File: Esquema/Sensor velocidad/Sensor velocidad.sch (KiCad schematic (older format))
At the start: 1 part

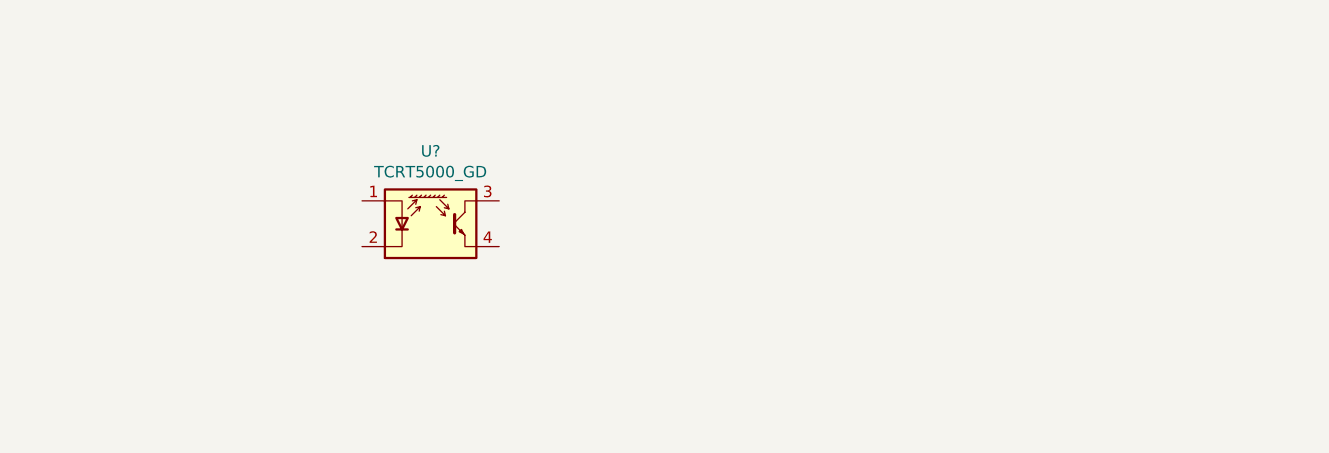
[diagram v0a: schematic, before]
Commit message: Coloco componentes en esquema.
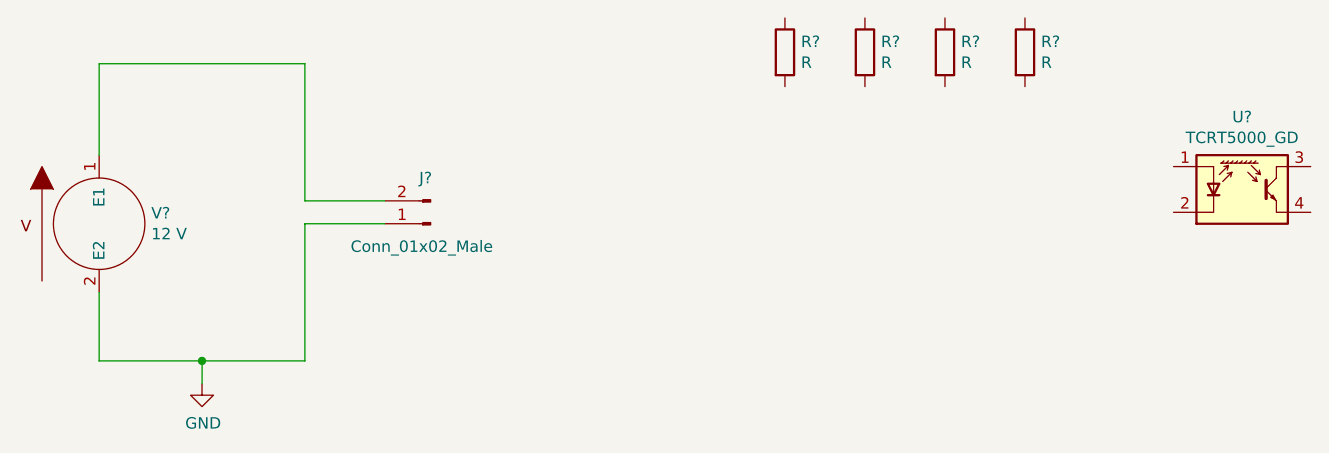
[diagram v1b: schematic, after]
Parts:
- added J?: Conn_01x02_Male, symbol Connector:Conn_01x02_Male
- added R? (x4): R, symbol Device:R
- added V?: 12 V, symbol pspice:VSOURCE
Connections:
- new net: J?.2 (Pin_2), V?.1 (E1)
- new net GND: J?.1 (Pin_1), V?.2 (E2)
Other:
- moved on the sheet: U?
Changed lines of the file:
@@
 EESchema Schematic File Version 4
-EELAYER 30 0
+LIBS:Sensor velocidad-cache
+EELAYER 29 0
 EELAYER END
 $Descr A4 11693 8268
@@
 L Sensor_vel_bib:TCRT5000_GD U?
 U 1 1 5D8A6EC4
-P 4450 2250
-F 0 "U?" H 4450 2567 50  0000 C CNN
-F 1 "TCRT5000_GD" H 4450 2476 50  0000 C CNN
-F 2 "" H 4450 2050 50  0001 C CNN
-F 3 "https://www.vishay.com/docs/83760/tcrt5000.pdf" H 4450 2350 50  0001 C CNN
-	1    4450 2250
+P 8000 2100
+F 0 "U?" H 8000 2417 50  0000 C CNN
+F 1 "TCRT5000_GD" H 8000 2326 50  0000 C CNN
+F 2 "" H 8000 1900 50  0001 C CNN
+F 3 "https://www.vishay.com/docs/83760/tcrt5000.pdf" H 8000 2200 50  0001 C CNN
+	1    8000 2100
 	1    0    0    -1
 $EndComp
+$Comp
+L pspice:VSOURCE V?
+U 1 1 5EBDBC13
+P 3000 2250
+F 0 "V?" H 3228 2296 50  0000 L CNN
+F 1 "12 V" H 3228 2205 50  0000 L CNN
+F 2 "" H 3000 2250 50  0001 C CNN
+F 3 "~" H 3000 2250 50  0001 C CNN
+	1    3000 2250
+	1    0    0    -1
+$EndComp
+$Comp
+L Connector:Conn_01x02_Male J?
+U 1 1 5EBDCBA0
+P 4450 2250
+F 0 "J?" H 4500 2050 50  0000 R CNN
+F 1 "Conn_01x02_Male" H 4800 2350 50  0000 R CNN
+F 2 "" H 4450 2250 50  0001 C CNN
+F 3 "~" H 4450 2250 50  0001 C CNN
+	1    4450 2250
+	-1   0    0    1
+$EndComp
+Wire Wire Line
+	3000 1950 3000 1550
+Wire Wire Line
+	3000 1550 3900 1550
+Wire Wire Line
+	3900 1550 3900 2150
+Wire Wire Line
+	3900 2150 4250 2150
+Wire Wire Line
+	3000 2550 3000 2850
+Wire Wire Line
+	3000 2850 3450 2850
+Wire Wire Line
+	3900 2850 3900 2250
+Wire Wire Line
+	3900 2250 4250 2250
+$Comp
+L power:GND #PWR?
+U 1 1 5EBDEA39
+P 3450 2950
+F 0 "#PWR?" H 3450 2700 50  0001 C CNN
+F 1 "GND" H 3455 2777 50  0000 C CNN
+F 2 "" H 3450 2950 50  0001 C CNN
+F 3 "" H 3450 2950 50  0001 C CNN
+	1    3450 2950
+	1    0    0    -1
+$EndComp
+Wire Wire Line
+	3450 2950 3450 2850
+Connection ~ 3450 2850
+Wire Wire Line
+	3450 2850 3900 2850
+$Comp
+L Device:R R?
+U 1 1 5EBDFE75
+P 6000 1500
+F 0 "R?" H 6070 1546 50  0000 L CNN
+F 1 "R" H 6070 1455 50  0000 L CNN
+F 2 "" V 5930 1500 50  0001 C CNN
+F 3 "~" H 6000 1500 50  0001 C CNN
+	1    6000 1500
+	1    0    0    -1
+$EndComp
+$Comp
+L Device:R R?
+U 1 1 5EBE000A
+P 6350 1500
+F 0 "R?" H 6420 1546 50  0000 L CNN
+F 1 "R" H 6420 1455 50  0000 L CNN
+F 2 "" V 6280 1500 50  0001 C CNN
+F 3 "~" H 6350 1500 50  0001 C CNN
+	1    6350 1500
+	1    0    0    -1
+$EndComp
+$Comp
+L Device:R R?
+U 1 1 5EBE01EF
+P 6700 1500
+F 0 "R?" H 6770 1546 50  0000 L CNN
+F 1 "R" H 6770 1455 50  0000 L CNN
+F 2 "" V 6630 1500 50  0001 C CNN
+F 3 "~" H 6700 1500 50  0001 C CNN
+	1    6700 1500
+	1    0    0    -1
+$EndComp
+$Comp
+L Device:R R?
+U 1 1 5EBE04B6
+P 7050 1500
+F 0 "R?" H 7120 1546 50  0000 L CNN
+F 1 "R" H 7120 1455 50  0000 L CNN
+F 2 "" V 6980 1500 50  0001 C CNN
+F 3 "~" H 7050 1500 50  0001 C CNN
+	1    7050 1500
+	1    0    0    -1
+$EndComp

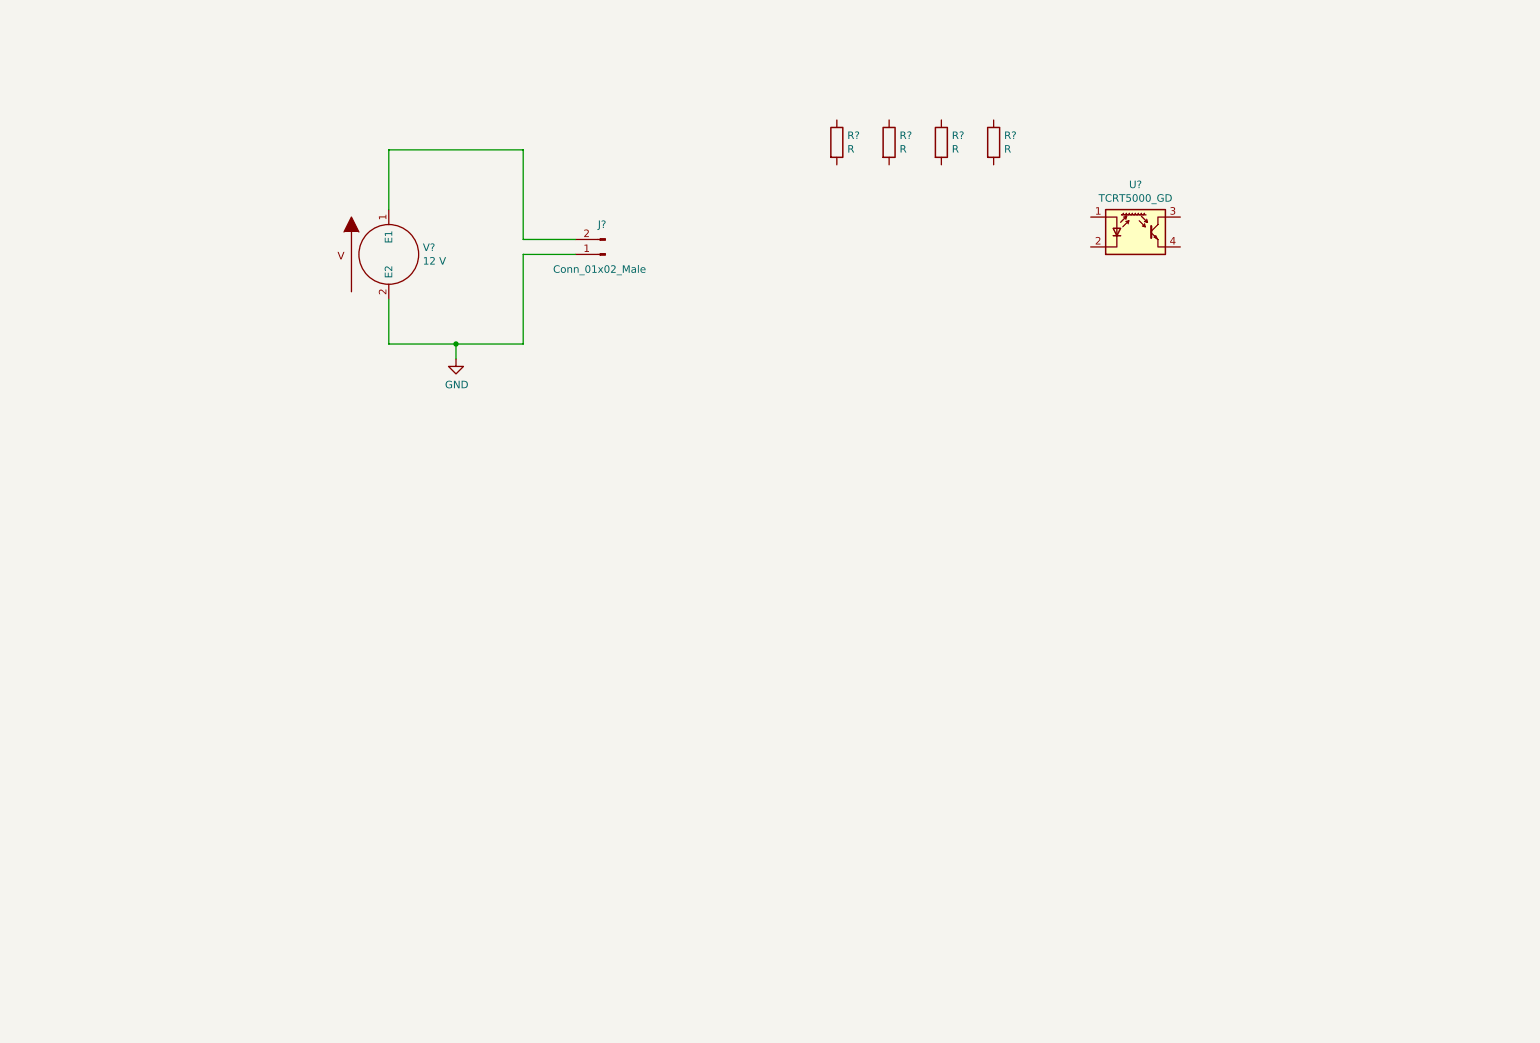
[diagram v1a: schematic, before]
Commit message: Avance sobre esquemático, agregué sensores y conectores
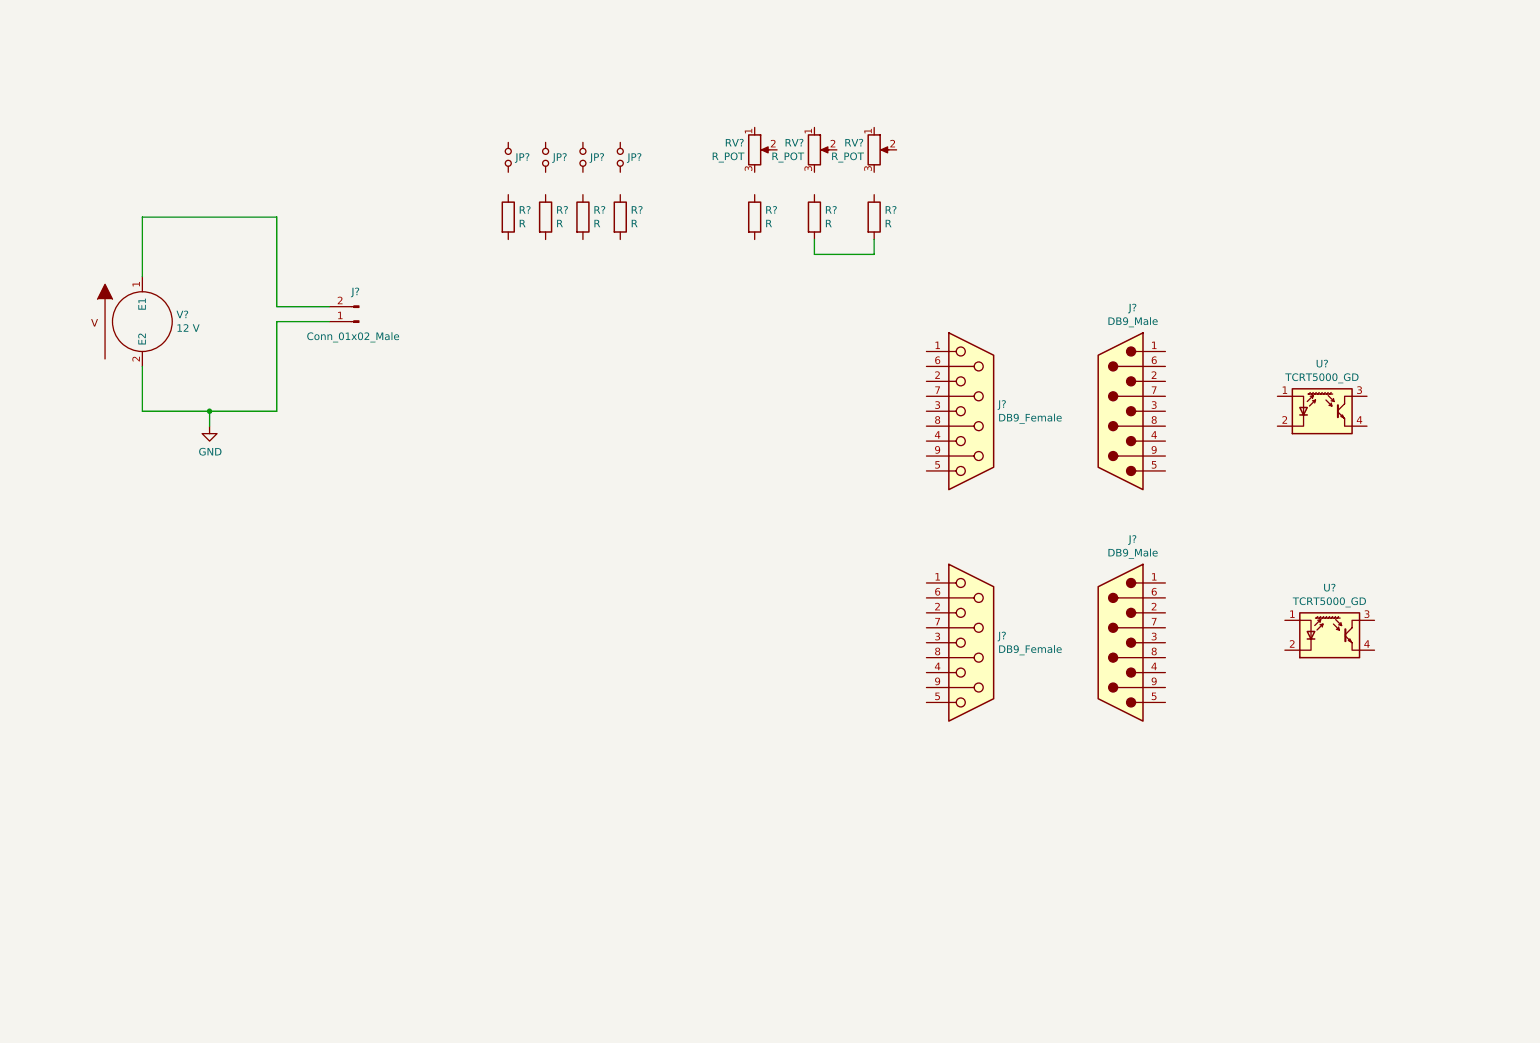
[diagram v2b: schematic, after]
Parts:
- added J? (x2): DB9_Female, symbol Connector:DB9_Female
- added J? (x2): DB9_Male, symbol Connector:DB9_Male
- added JP? (x4): Jumper_NO_Small, symbol Device:Jumper_NO_Small
- added R? (x3): R, symbol Device:R
- added RV? (x3): R_POT, symbol Device:R_POT
- added U?: TCRT5000_GD, symbol Sensor_vel_bib:TCRT5000_GD
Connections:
- new net: R?.2, R?.2
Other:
- moved on the sheet: J?, R?, U?, V?

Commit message: Agregué componentes y a los componentes sus funciones (a la mayoría)
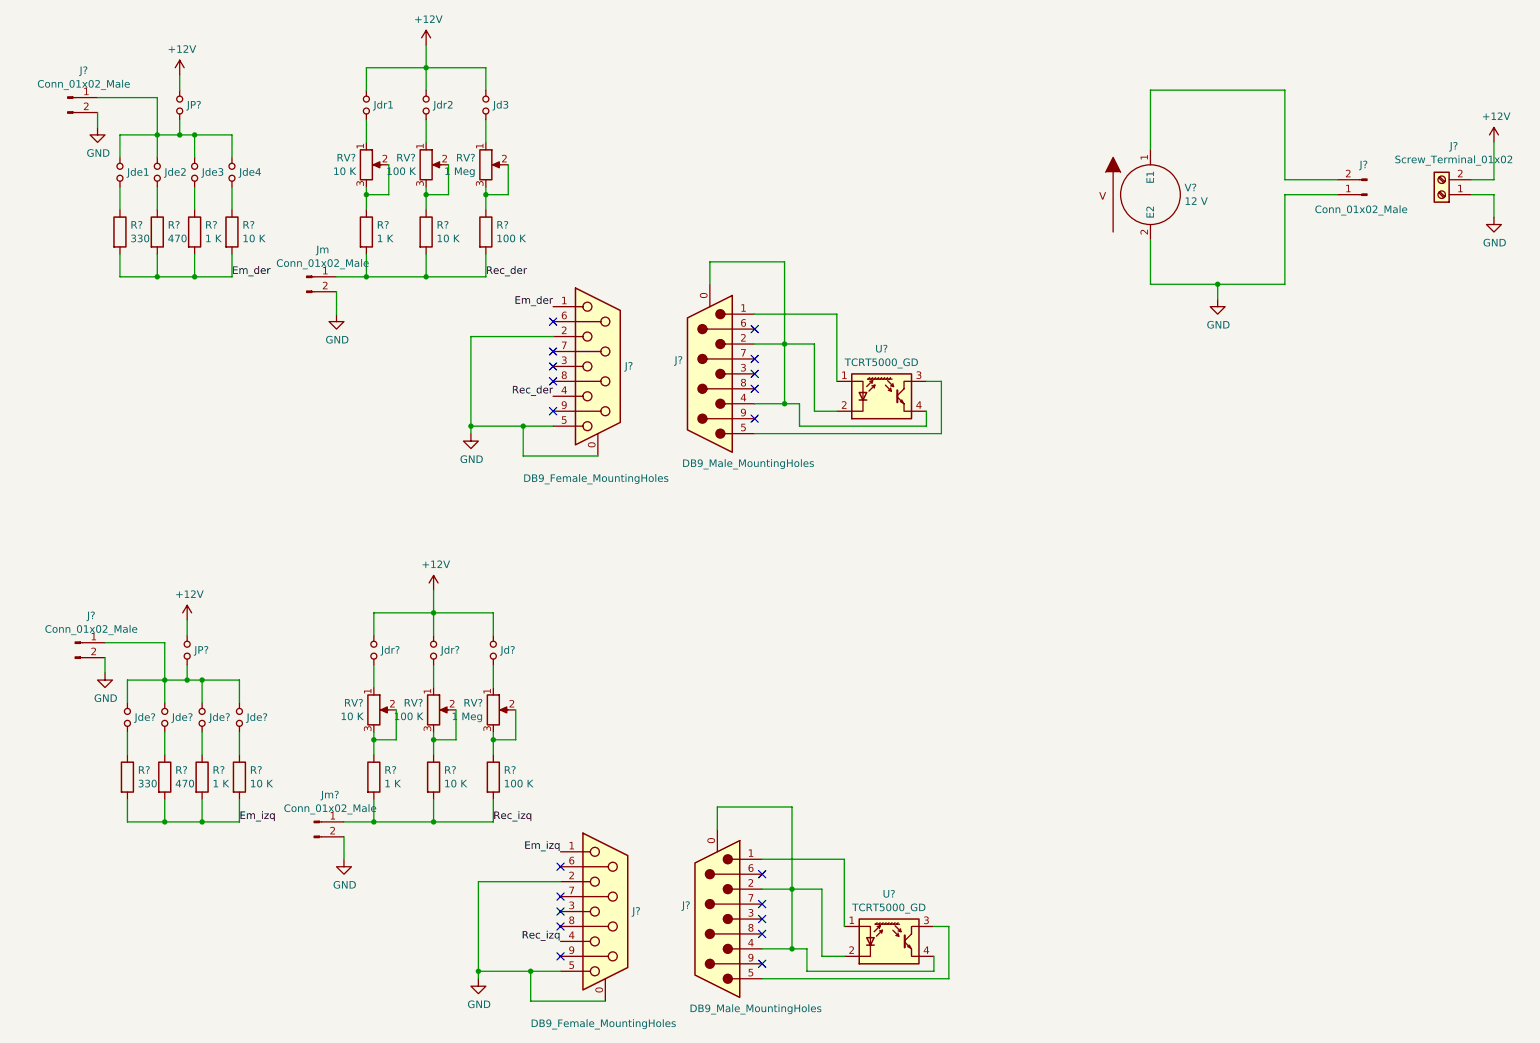
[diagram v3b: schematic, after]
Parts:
- removed J? (x2): DB9_Female, symbol Connector:DB9_Female
- removed J? (x2): DB9_Male, symbol Connector:DB9_Male
- removed U?: TCRT5000_GD, symbol Sensor_vel_bib:TCRT5000_GD
- added J? (x2): DB9_Female_MountingHoles, symbol Connector:DB9_Female_MountingHoles
- added J? (x2): DB9_Male_MountingHoles, symbol Connector:DB9_Male_MountingHoles
- added J?: Screw_Terminal_01x02, symbol Connector:Screw_Terminal_01x02
- added J? (x2), Jm, Jm?: Conn_01x02_Male, symbol Connector:Conn_01x02_Male
- added JP? (x2), Jd3, Jd?, Jde? (x4), Jdr1, Jdr2, Jdr? (x2): Jumper_NO_Small, symbol Device:Jumper_NO_Small
- added R?: 330, symbol Device:R
- added R?: 470, symbol Device:R
- added R? (x2): 1 K, symbol Device:R
- added R? (x2): 10 K, symbol Device:R
- added R?: 100 K, symbol Device:R
- added RV?: 10 K, symbol Device:R_POT
- added RV?: 100 K, symbol Device:R_POT
- added RV?: 1 Meg, symbol Device:R_POT
- added U?: TCRT5000_GD, symbol Sensor_vel_bib:TCRT5000_GD
- Jde1, Jde4: renamed from JP?; Función (none) -> Configuración de R 330 Ohm
- Jde2: renamed from JP?; Función (none) -> Configuración de R 470 Ohm
- Jde3: renamed from JP?; Función (none) -> Configuración de R 1 KOhm
- R?: value R -> 330; Función (none) -> Resistencia para configurar corriente 1
- R?: value R -> 470; Función (none) -> Resistencia para configurar corriente 2
- R?: value R -> 1 K; Función (none) -> Resistencia para configurar corriente 3
- R?: value R -> 10 K; Función (none) -> Resistencia para configurar corriente 4
- R?: value R -> 1 K; Función (none) -> Configuración R mínima para medición de sensor óptico
- R?: value R -> 10 K; Función (none) -> Configuración R mínima para medición de sensor óptico
- R?: value R -> 100 K; Función (none) -> Configuración R mínima para medición de sensor óptico
- RV?: value R_POT -> 10 K; Función (none) -> Reóstato ajuste de caída de tensión en medición
- RV?: value R_POT -> 100 K; Función (none) -> Reóstato ajuste de caída de tensión en medición
- RV?: value R_POT -> 1 Meg; Función (none) -> Reóstato ajuste de caída de tensión en medición
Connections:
- net GND: now also J?.0 (PAD), J?.0 (PAD), J?.1 (Pin_1), J?.2, J?.2, J?.2 (Pin_2), J?.2 (Pin_2), J?.5, J?.5, Jm.2 (Pin_2), Jm?.2 (Pin_2)
- net at U?.1 (A): now also J?.1
- net at U?.2 (K): now also U?.4 (E), J?.0 (PAD), J?.2, J?.4
- net at U?.3 (C): now also J?.5
- net at R?.1: now also Jde1.2
- net Em_der: now reaches R?.2
- net Em_der: now also R?.2, R?.2, R?.2, J?.1
- net at R?.1: now also Jde2.2
- net at R?.1: now also Jde3.2
- net at R?.1: now also Jde4.2
- net at Jde1.1: now also Jde2.1, Jde3.1, Jde4.1, J?.1 (Pin_1), JP?.2
- net at R?.1: now also RV?.2, RV?.3 (x3)
- net Rec_der: now reaches R?.2
- net Rec_der: now also R?.2, R?.2, J?.4, Jm.1 (Pin_1)
- net at RV?.1: now also Jdr1.2
- net at RV?.1: now also Jdr2.2
- net at RV?.1: now also Jd3.2
- new net: J?.1, U?.1 (A)
- new net: J?.0 (PAD), J?.2, J?.4, U?.2 (K), U?.4 (E)
- new net: J?.5, U?.3 (C)
- new net: Jde?.2, R?.1 (x4)
- new net: J?.1 (Pin_1), JP?.2, Jde?.1, Jde?.1, Jde?.1, Jde?.1
- new net: R?.1, RV?.2, RV?.3 (x3)
- new net: Jdr?.2, RV?.1 (x2)
- new net: Jd?.2, RV?.1
- new net +12V: J?.2 (Pin_2), JP?.1, JP?.1, Jd3.1, Jd?.1, Jdr1.1, Jdr2.1, Jdr?.1, Jdr?.1
- new net Em_izq: J?.1, R?.2, R?.2, R?.2, R?.2
- new net Rec_izq: J?.4, Jm?.1 (Pin_1), R?.2, R?.2, R?.2
- no-connect marks 0 -> 20
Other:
- moved on the sheet: J?, Jde1, Jde2, Jde3, Jde4, R?, RV?, U?, V?
